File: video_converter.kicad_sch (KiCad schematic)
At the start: 76 parts, among them J1 S4B-ZR-SM4A-TF(LF)(SN), J2 Conn_01x09_Male, J3 Conn_02x06_Odd_Even, J4 Conn_02x06_Odd_Even, J5 Conn_02x06_Odd_Even, J6 2-1734592-4, J7 Screw_Terminal_01x02, SW1 SW_DIP_x02, U1 ADV7180BSTZ, U2 AMS1117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

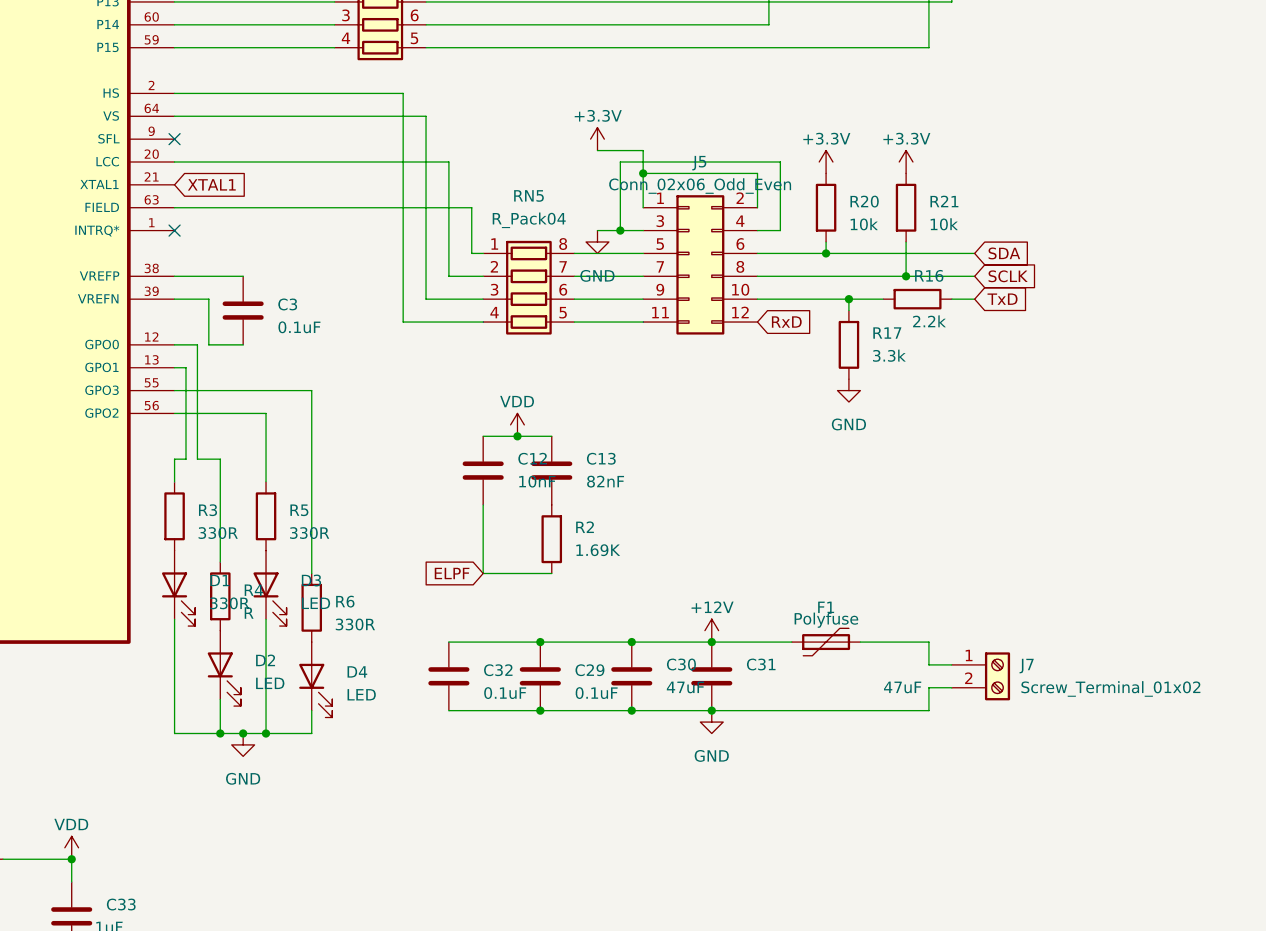
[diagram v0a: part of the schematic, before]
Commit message: updated layout
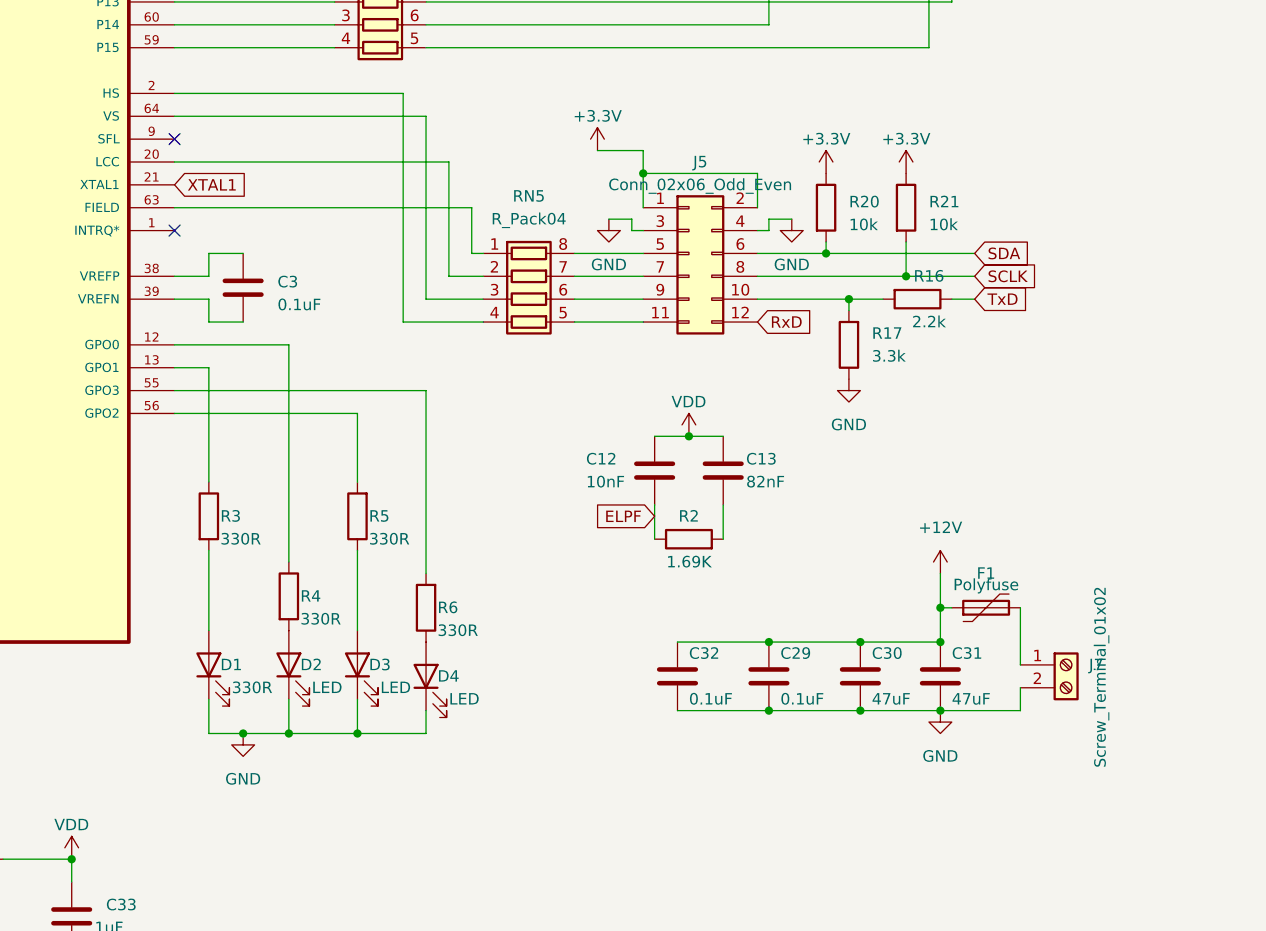
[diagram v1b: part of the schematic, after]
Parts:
- R4: value R -> 330R
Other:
- moved on the sheet: C12, C13, C29, C3, C30, C31, C32, D1, D2, D3, D4, F1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

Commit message: fixed bad routing
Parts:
- added R22: (no value), symbol Device:R
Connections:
- net at C18.2, U1.35 (AIN1): now also R22.2
- net at C19.2, C24.2, U1.36 (AIN2): now also R22.1
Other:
- moved on the sheet: C25, C26, C27, C28, J1, J2, J6, R11, R13, R8
